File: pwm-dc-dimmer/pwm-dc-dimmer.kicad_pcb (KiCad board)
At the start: 2 copper layers, 61 x 125.5 mm, 90 parts, among them J1 Screw_Terminal_01x02, J10 Screw_Terminal_01x02, J11 Screw_Terminal_01x02, J12 Screw_Terminal_01x02, J13 Screw_Terminal_01x02, J14 Conn_02x03_Odd_Even, J15 Conn_02x03_Odd_Even, J2 Screw_Terminal_01x02, J3 Screw_Terminal_01x02, J4 Screw_Terminal_01x02, J5 Screw_Terminal_01x02, J6 Screw_Terminal_01x02, J7 Screw_Terminal_01x02, J8 Screw_Terminal_01x02, J9 Screw_Terminal_01x02, Q1 Q_NMOS_GDS, Q10 Q_NMOS_GDS, Q11 Q_NMOS_GDS, Q12 Q_NMOS_GDS, Q2 Q_NMOS_GDS, Q3 Q_NMOS_GDS, Q4 Q_NMOS_GDS, Q5 Q_NMOS_GDS, Q6 Q_NMOS_GDS, Q7 Q_NMOS_GDS, Q8 Q_NMOS_GDS, Q9 Q_NMOS_GDS

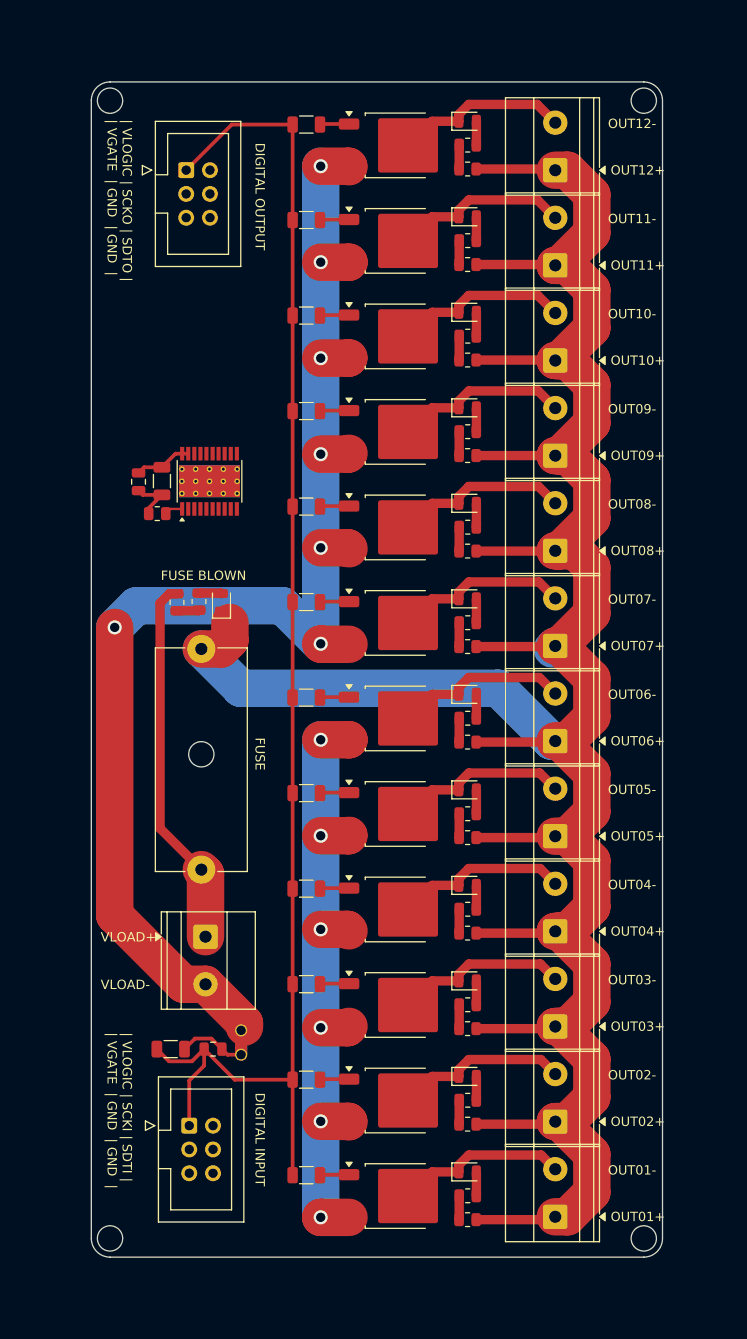
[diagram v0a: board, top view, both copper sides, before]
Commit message: Optimize base routing
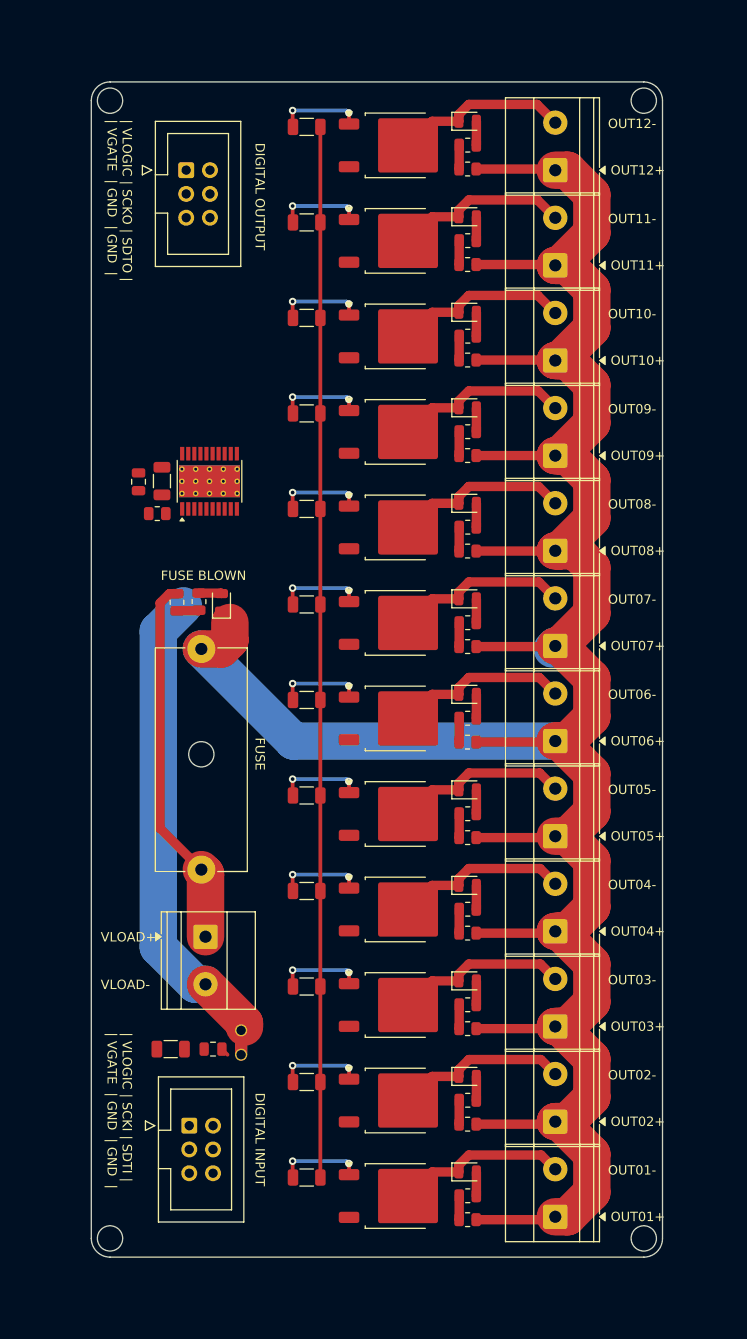
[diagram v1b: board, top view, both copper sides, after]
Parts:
- moved R10 0.25 mm to (105.5, 91.9), turned to 180 degrees
- moved R11 0.25 mm to (105.5, 81.7), turned to 180 degrees
- moved R12 0.25 mm to (105.5, 71.5), turned to 180 degrees
- moved R13 0.25 mm to (105.5, 61.3), turned to 180 degrees
- moved R2 0.25 mm to (105.5, 163.3), turned to 180 degrees
- moved R3 0.25 mm to (105.5, 173.5), turned to 180 degrees
- moved R4 0.25 mm to (105.5, 153.1), turned to 180 degrees
- moved R5 0.25 mm to (105.5, 142.9), turned to 180 degrees
- moved R6 0.25 mm to (105.5, 132.7), turned to 180 degrees
- moved R7 0.25 mm to (105.5, 122.5), turned to 180 degrees
- moved R8 0.25 mm to (105.5, 112.3), turned to 180 degrees
- moved R9 0.25 mm to (105.5, 102.1), turned to 180 degrees
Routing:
- net GND_LOAD: track 213.0 -> 50.5 mm, vias 13 -> 0
- net V_GATE: track 151.3 -> 113.1 mm
- net GND: track 12.5 -> 0.85 mm
- net V_LOGIC: track 6.16 -> 0.00 mm
- net GATE_SINK_5: track 3.12 -> 9.07 mm, vias 0 -> 2
- net GATE_SINK_8: track 3.12 -> 9.07 mm, vias 0 -> 2
- net GATE_SINK_7: track 3.12 -> 9.07 mm, vias 0 -> 2
- net GATE_SINK_12: track 3.12 -> 9.07 mm, vias 0 -> 2
- net GATE_SINK_9: track 3.12 -> 9.07 mm, vias 0 -> 2
- net GATE_SINK_6: track 3.12 -> 9.07 mm, vias 0 -> 2
- net GATE_SINK_4: track 3.12 -> 9.07 mm, vias 0 -> 2
- net GATE_SINK_3: track 3.12 -> 9.07 mm, vias 0 -> 2
- net GATE_SINK_2: track 3.12 -> 9.07 mm, vias 0 -> 2
- net GATE_SINK_11: track 3.12 -> 9.07 mm, vias 0 -> 2
- net GATE_SINK_10: track 3.12 -> 9.07 mm, vias 0 -> 2
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
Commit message: Finish routing
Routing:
- net GND_LOAD: track 50.5 -> 218.4 mm, vias 0 -> 11
- net GND: track 0.85 -> 157.0 mm
- net V_LOGIC: track 0.00 -> 155.1 mm, vias 0 -> 1
- net GATE_SINK_1: track 9.07 -> 91.9 mm, vias 2 -> 3
- net SDTI: track 0.00 -> 82.2 mm, vias 0 -> 2
- net SCKI: track 0.00 -> 73.8 mm
- net GATE_SINK_2: track 9.07 -> 74.7 mm, vias 2 -> 3
- net V_GATE: track 113.1 -> 173.4 mm, vias 0 -> 2
- net GATE_SINK_3: track 9.07 -> 63.1 mm, vias 2 -> 3
- net GATE_SINK_12: track 9.07 -> 56.6 mm, vias 2 -> 3
- net GATE_SINK_4: track 9.07 -> 55.1 mm, vias 2 -> 3
- net GATE_SINK_11: track 9.07 -> 42.4 mm, vias 2 -> 3
- net GATE_SINK_5: track 9.07 -> 41.4 mm, vias 2 -> 3
- net SCKO: track 0.00 -> 29.3 mm
- net SDTO: track 0.00 -> 26.6 mm
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
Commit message: Finalize DC dimmer v0.1
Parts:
- added G***: LOGO, LOGO, F.Cu at (95.5, 85.8)
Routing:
- added copper zone on B.Cu, net GND
- added copper zone on F.Cu, net GND
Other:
- board text added: "DC Dimmer v0.1 | github.com/niliha"
- board text added: "JLCJLCJLCJLC"
